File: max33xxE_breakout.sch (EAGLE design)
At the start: 4 parts

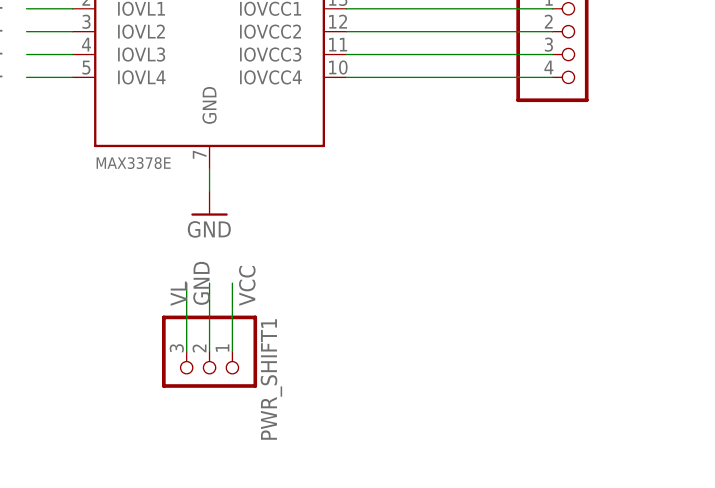
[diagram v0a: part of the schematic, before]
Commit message: rename the power segments too
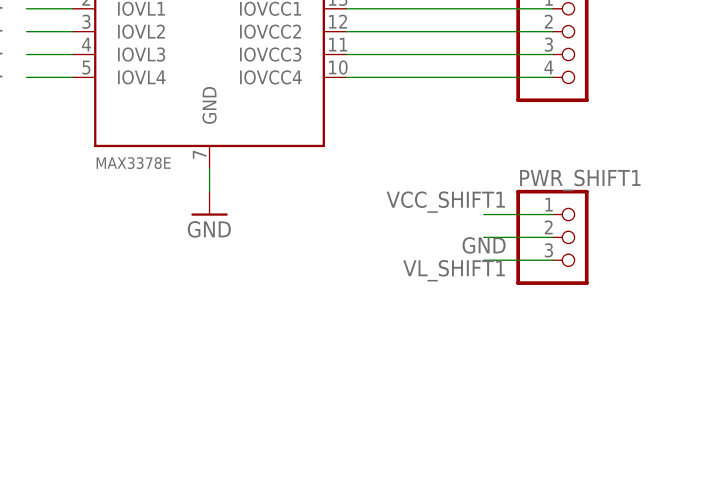
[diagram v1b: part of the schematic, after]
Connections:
- net VCC renamed VCC_SHIFT1
- net VL renamed VL_SHIFT1
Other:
- moved on the sheet: PWR_SHIFT1
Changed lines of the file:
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@@
 <instance part="P+1" gate="1" x="35.56" y="66.04"/>
 <instance part="+3V1" gate="G$1" x="30.48" y="66.04"/>
-<instance part="PWR_SHIFT1" gate="A" x="33.02" y="5.08" rot="R270"/>
+<instance part="PWR_SHIFT1" gate="A" x="73.66" y="20.32"/>
 <instance part="IOVCC_SHIFT1" gate="A" x="73.66" y="40.64"/>
 <instance part="IOVL_SHIFT1" gate="A" x="73.66" y="60.96"/>
@@
 <segment>
 <pinref part="PWR_SHIFT1" gate="A" pin="2"/>
-<wire x1="33.02" y1="7.62" x2="33.02" y2="15.24" width="0.1524" layer="91"/>
-<label x="33.02" y="12.7" size="1.778" layer="95" rot="R90"/>
+<wire x1="71.12" y1="20.32" x2="63.5" y2="20.32" width="0.1524" layer="91"/>
+<label x="66.04" y="20.32" size="1.778" layer="95" rot="R180"/>
 </segment>
 </net>
-<net name="VCC" class="0">
+<net name="VCC_SHIFT1" class="0">
 <segment>
 <pinref part="SHIFT1" gate="G$1" pin="VCC"/>
@@
 <segment>
 <pinref part="PWR_SHIFT1" gate="A" pin="1"/>
-<wire x1="35.56" y1="7.62" x2="35.56" y2="15.24" width="0.1524" layer="91"/>
-<label x="38.1" y="12.7" size="1.778" layer="95" rot="R90"/>
+<wire x1="71.12" y1="22.86" x2="63.5" y2="22.86" width="0.1524" layer="91"/>
+<label x="66.04" y="25.4" size="1.778" layer="95" rot="R180"/>
 </segment>
 </net>
-<net name="VL" class="0">
+<net name="VL_SHIFT1" class="0">
 <segment>
 <pinref part="SHIFT1" gate="G$1" pin="VL"/>
@@
 <segment>
 <pinref part="PWR_SHIFT1" gate="A" pin="3"/>
-<wire x1="30.48" y1="7.62" x2="30.48" y2="15.24" width="0.1524" layer="91"/>
-<label x="30.48" y="12.7" size="1.778" layer="95" rot="R90"/>
+<wire x1="71.12" y1="17.78" x2="63.5" y2="17.78" width="0.1524" layer="91"/>
+<label x="66.04" y="17.78" size="1.778" layer="95" rot="R180"/>
 </segment>
 </net>

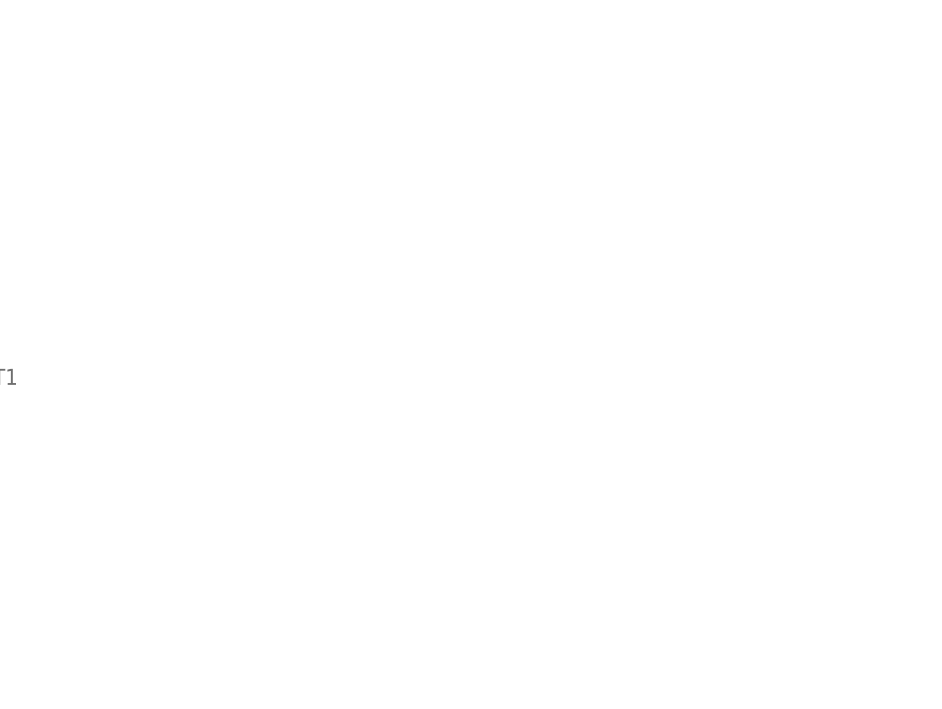
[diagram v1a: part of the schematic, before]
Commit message: apparently the automatic net rename when copying does not quite work if the nets are not actually drawn all the way through
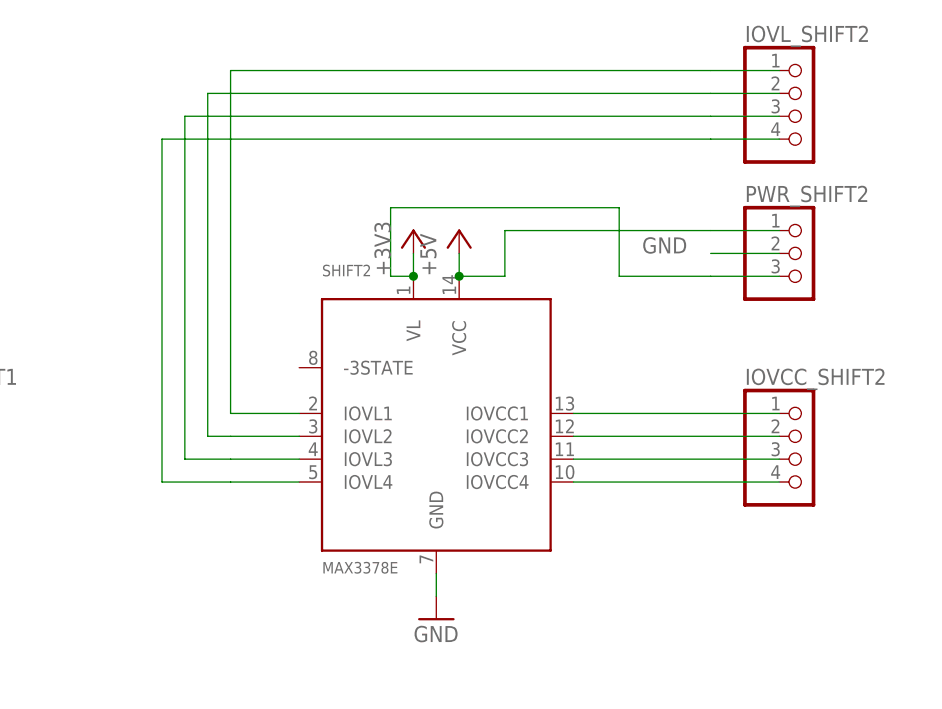
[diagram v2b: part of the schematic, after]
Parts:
- added IOVCC_SHIFT2, IOVL_SHIFT2: (no value), pinhead:PINHD-1X4
- added PWR_SHIFT2: (no value), pinhead:PINHD-1X3
- added SHIFT2: MAX3378E, max33xxE_lvl_shifters:MAX3378E
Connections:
- new net IOVCC1_SHIFT2: IOVCC_SHIFT2.1, SHIFT2.IOVCC1
- new net IOVCC2_SHIFT2: IOVCC_SHIFT2.2, SHIFT2.IOVCC2
- new net IOVCC3_SHIFT2: IOVCC_SHIFT2.3, SHIFT2.IOVCC3
- new net IOVCC4_SHIFT2: IOVCC_SHIFT2.4, SHIFT2.IOVCC4
- new net IOVL1_SHIFT2: IOVL_SHIFT2.1, SHIFT2.IOVL1
- new net IOVL2_SHIFT2: IOVL_SHIFT2.2, SHIFT2.IOVL2
- new net IOVL3_SHIFT2: IOVL_SHIFT2.3, SHIFT2.IOVL3
- new net IOVL4_SHIFT2: IOVL_SHIFT2.4, SHIFT2.IOVL4
- new net VCC_SHIFT2: PWR_SHIFT2.1, SHIFT2.VCC
- new net VL_SHIFT2: PWR_SHIFT2.3, SHIFT2.VL
- net GND: now also PWR_SHIFT2.2, SHIFT2.GND
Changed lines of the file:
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@@
 <part name="IOVCC_SHIFT1" library="pinhead" deviceset="PINHD-1X4" device=""/>
 <part name="IOVL_SHIFT1" library="pinhead" deviceset="PINHD-1X4" device=""/>
+<part name="SHIFT2" library="max33xxE_lvl_shifters" deviceset="MAX3378E" device=""/>
+<part name="GND2" library="supply1" deviceset="GND" device=""/>
+<part name="P+2" library="supply1" deviceset="+5V" device=""/>
+<part name="+3V2" library="supply1" deviceset="+3V3" device=""/>
+<part name="PWR_SHIFT2" library="pinhead" deviceset="PINHD-1X3" device=""/>
+<part name="IOVCC_SHIFT2" library="pinhead" deviceset="PINHD-1X4" device=""/>
+<part name="IOVL_SHIFT2" library="pinhead" deviceset="PINHD-1X4" device=""/>
 </parts>
 <sheets>
@@
 <instance part="IOVCC_SHIFT1" gate="A" x="73.66" y="40.64"/>
 <instance part="IOVL_SHIFT1" gate="A" x="73.66" y="60.96"/>
+<instance part="SHIFT2" gate="G$1" x="129.54" y="43.18"/>
+<instance part="GND2" gate="1" x="129.54" y="22.86"/>
+<instance part="P+2" gate="1" x="132.08" y="66.04"/>
+<instance part="+3V2" gate="G$1" x="127" y="66.04"/>
+<instance part="PWR_SHIFT2" gate="A" x="170.18" y="63.5"/>
+<instance part="IOVCC_SHIFT2" gate="A" x="170.18" y="40.64"/>
+<instance part="IOVL_SHIFT2" gate="A" x="170.18" y="78.74"/>
 </instances>
 <busses>
@@
 <label x="66.04" y="20.32" size="1.778" layer="95" rot="R180"/>
 </segment>
+<segment>
+<pinref part="SHIFT2" gate="G$1" pin="GND"/>
+<pinref part="GND2" gate="1" pin="GND"/>
+<wire x1="129.54" y1="25.4" x2="129.54" y2="27.94" width="0.1524" layer="91"/>
+</segment>
+<segment>
+<pinref part="PWR_SHIFT2" gate="A" pin="2"/>
+<wire x1="167.64" y1="63.5" x2="160.02" y2="63.5" width="0.1524" layer="91"/>
+<label x="152.4" y="63.5" size="1.778" layer="95"/>
+</segment>
 </net>
 <net name="VCC_SHIFT1" class="0">
@@
 </segment>
 </net>
+<net name="IOVCC4_SHIFT2" class="0">
+<segment>
+<pinref part="SHIFT2" gate="G$1" pin="IOVCC4"/>
+<pinref part="IOVCC_SHIFT2" gate="A" pin="4"/>
+<wire x1="144.78" y1="38.1" x2="167.64" y2="38.1" width="0.1524" layer="91"/>
+</segment>
+</net>
+<net name="IOVCC3_SHIFT2" class="0">
+<segment>
+<pinref part="SHIFT2" gate="G$1" pin="IOVCC3"/>
+<pinref part="IOVCC_SHIFT2" gate="A" pin="3"/>
+<wire x1="144.78" y1="40.64" x2="167.64" y2="40.64" width="0.1524" layer="91"/>
+</segment>
+</net>
+<net name="IOVCC2_SHIFT2" class="0">
+<segment>
+<pinref part="SHIFT2" gate="G$1" pin="IOVCC2"/>
+<pinref part="IOVCC_SHIFT2" gate="A" pin="2"/>
+<wire x1="144.78" y1="43.18" x2="167.64" y2="43.18" width="0.1524" layer="91"/>
+</segment>
+</net>
+<net name="IOVCC1_SHIFT2" class="0">
+<segment>
+<pinref part="SHIFT2" gate="G$1" pin="IOVCC1"/>
+<pinref part="IOVCC_SHIFT2" gate="A" pin="1"/>
+<wire x1="144.78" y1="45.72" x2="167.64" y2="45.72" width="0.1524" layer="91"/>
+</segment>
+</net>
+<net name="IOVL2_SHIFT2" class="0">
+<segment>
+<pinref part="IOVL_SHIFT2" gate="A" pin="2"/>
+<wire x1="167.64" y1="81.28" x2="160.02" y2="81.28" width="0.1524" layer="91"/>
+<wire x1="160.02" y1="81.28" x2="104.14" y2="81.28" width="0.1524" layer="91"/>
+<wire x1="104.14" y1="81.28" x2="104.14" y2="43.18" width="0.1524" layer="91"/>
+<pinref part="SHIFT2" gate="G$1" pin="IOVL2"/>
+<wire x1="114.3" y1="43.18" x2="106.68" y2="43.18" width="0.1524" layer="91"/>
+<wire x1="104.14" y1="43.18" x2="106.68" y2="43.18" width="0.1524" layer="91"/>
+</segment>
+</net>
+<net name="IOVL1_SHIFT2" class="0">
+<segment>
+<pinref part="IOVL_SHIFT2" gate="A" pin="1"/>
+<wire x1="167.64" y1="83.82" x2="160.02" y2="83.82" width="0.1524" layer="91"/>
+<pinref part="SHIFT2" gate="G$1" pin="IOVL1"/>
+<wire x1="114.3" y1="45.72" x2="106.68" y2="45.72" width="0.1524" layer="91"/>
+<wire x1="160.02" y1="83.82" x2="106.68" y2="83.82" width="0.1524" layer="91"/>
+<wire x1="106.68" y1="83.82" x2="106.68" y2="45.72" width="0.1524" layer="91"/>
+</segment>
+</net>
+<net name="IOVL3_SHIFT2" class="0">
+<segment>
+<pinref part="IOVL_SHIFT2" gate="A" pin="3"/>
+<wire x1="167.64" y1="78.74" x2="160.02" y2="78.74" width="0.1524" layer="91"/>
+<wire x1="160.02" y1="78.74" x2="101.6" y2="78.74" width="0.1524" layer="91"/>
+<wire x1="101.6" y1="78.74" x2="101.6" y2="40.64" width="0.1524" layer="91"/>
+<pinref part="SHIFT2" gate="G$1" pin="IOVL3"/>
+<wire x1="114.3" y1="40.64" x2="106.68" y2="40.64" width="0.1524" layer="91"/>
+<wire x1="101.6" y1="40.64" x2="106.68" y2="40.64" width="0.1524" layer="91"/>
+</segment>
+</net>
+<net name="IOVL4_SHIFT2" class="0">
+<segment>
+<pinref part="IOVL_SHIFT2" gate="A" pin="4"/>
+<wire x1="167.64" y1="76.2" x2="160.02" y2="76.2" width="0.1524" layer="91"/>
+<wire x1="160.02" y1="76.2" x2="99.06" y2="76.2" width="0.1524" layer="91"/>
+<wire x1="99.06" y1="76.2" x2="99.06" y2="38.1" width="0.1524" layer="91"/>
+<pinref part="SHIFT2" gate="G$1" pin="IOVL4"/>
+<wire x1="114.3" y1="38.1" x2="106.68" y2="38.1" width="0.1524" layer="91"/>
+<wire x1="99.06" y1="38.1" x2="106.68" y2="38.1" width="0.1524" layer="91"/>
+</segment>
+</net>
+<net name="VL_SHIFT2" class="0">
+<segment>
+<pinref part="SHIFT2" gate="G$1" pin="VL"/>
+<pinref part="+3V2" gate="G$1" pin="+3V3"/>
+<wire x1="127" y1="63.5" x2="127" y2="60.96" width="0.1524" layer="91"/>
+<pinref part="PWR_SHIFT2" gate="A" pin="3"/>
+<wire x1="167.64" y1="60.96" x2="160.02" y2="60.96" width="0.1524" layer="91"/>
+<wire x1="160.02" y1="60.96" x2="149.86" y2="60.96" width="0.1524" layer="91"/>
+<wire x1="149.86" y1="60.96" x2="149.86" y2="68.58" width="0.1524" layer="91"/>
+<wire x1="149.86" y1="68.58" x2="124.46" y2="68.58" width="0.1524" layer="91"/>
+<wire x1="124.46" y1="68.58" x2="124.46" y2="60.96" width="0.1524" layer="91"/>
+<wire x1="124.46" y1="60.96" x2="127" y2="60.96" width="0.1524" layer="91"/>
+<junction x="127" y="60.96"/>
+</segment>
+</net>
+<net name="VCC_SHIFT2" class="0">
+<segment>
+<pinref part="SHIFT2" gate="G$1" pin="VCC"/>
+<pinref part="P+2" gate="1" pin="+5V"/>
+<wire x1="132.08" y1="63.5" x2="132.08" y2="60.96" width="0.1524" layer="91"/>
+<pinref part="PWR_SHIFT2" gate="A" pin="1"/>
+<wire x1="167.64" y1="66.04" x2="160.02" y2="66.04" width="0.1524" layer="91"/>
+<wire x1="160.02" y1="66.04" x2="137.16" y2="66.04" width="0.1524" layer="91"/>
+<wire x1="137.16" y1="66.04" x2="137.16" y2="60.96" width="0.1524" layer="91"/>
+<wire x1="137.16" y1="60.96" x2="132.08" y2="60.96" width="0.1524" layer="91"/>
+<junction x="132.08" y="60.96"/>
+</segment>
+</net>

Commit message: quick first placement
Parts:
- added IOVCC_SHIFT3, IOVL_SHIFT3: (no value), pinhead:PINHD-1X4
- added PWR_SHIFT3: (no value), pinhead:PINHD-1X3
- added SHIFT3: MAX3378E, max33xxE_lvl_shifters:MAX3378E
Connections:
- new net IOVCC1_SHIFT3: IOVCC_SHIFT3.1, SHIFT3.IOVCC1
- new net IOVCC2_SHIFT3: IOVCC_SHIFT3.2, SHIFT3.IOVCC2
- new net IOVCC3_SHIFT3: IOVCC_SHIFT3.3, SHIFT3.IOVCC3
- new net IOVCC4_SHIFT3: IOVCC_SHIFT3.4, SHIFT3.IOVCC4
- new net IOVL1_SHIFT3: IOVL_SHIFT3.1, SHIFT3.IOVL1
- new net IOVL2_SHIFT3: IOVL_SHIFT3.2, SHIFT3.IOVL2
- new net IOVL3_SHIFT3: IOVL_SHIFT3.3, SHIFT3.IOVL3
- new net IOVL4_SHIFT3: IOVL_SHIFT3.4, SHIFT3.IOVL4
- new net VCC_SHIFT3: PWR_SHIFT3.1, SHIFT3.VCC
- new net VL_SHIFT3: PWR_SHIFT3.3, SHIFT3.VL
- net GND: now also PWR_SHIFT3.2, SHIFT3.GND
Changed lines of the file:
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@@
 <part name="IOVCC_SHIFT2" library="pinhead" deviceset="PINHD-1X4" device=""/>
 <part name="IOVL_SHIFT2" library="pinhead" deviceset="PINHD-1X4" device=""/>
+<part name="SHIFT3" library="max33xxE_lvl_shifters" deviceset="MAX3378E" device=""/>
+<part name="GND3" library="supply1" deviceset="GND" device=""/>
+<part name="P+3" library="supply1" deviceset="+5V" device=""/>
+<part name="+3V3" library="supply1" deviceset="+3V3" device=""/>
+<part name="PWR_SHIFT3" library="pinhead" deviceset="PINHD-1X3" device=""/>
+<part name="IOVCC_SHIFT3" library="pinhead" deviceset="PINHD-1X4" device=""/>
+<part name="IOVL_SHIFT3" library="pinhead" deviceset="PINHD-1X4" device=""/>
 </parts>
 <sheets>
@@
 <instance part="IOVCC_SHIFT2" gate="A" x="170.18" y="40.64"/>
 <instance part="IOVL_SHIFT2" gate="A" x="170.18" y="78.74"/>
+<instance part="SHIFT3" gate="G$1" x="226.06" y="38.1"/>
+<instance part="GND3" gate="1" x="226.06" y="17.78"/>
+<instance part="P+3" gate="1" x="228.6" y="60.96"/>
+<instance part="+3V3" gate="G$1" x="223.52" y="60.96"/>
+<instance part="PWR_SHIFT3" gate="A" x="266.7" y="58.42"/>
+<instance part="IOVCC_SHIFT3" gate="A" x="266.7" y="35.56"/>
+<instance part="IOVL_SHIFT3" gate="A" x="266.7" y="73.66"/>
 </instances>
 <busses>
@@
 <wire x1="167.64" y1="63.5" x2="160.02" y2="63.5" width="0.1524" layer="91"/>
 <label x="152.4" y="63.5" size="1.778" layer="95"/>
+</segment>
+<segment>
+<pinref part="SHIFT3" gate="G$1" pin="GND"/>
+<pinref part="GND3" gate="1" pin="GND"/>
+<wire x1="226.06" y1="20.32" x2="226.06" y2="22.86" width="0.1524" layer="91"/>
+</segment>
+<segment>
+<pinref part="PWR_SHIFT3" gate="A" pin="2"/>
+<wire x1="264.16" y1="58.42" x2="256.54" y2="58.42" width="0.1524" layer="91"/>
+<label x="248.92" y="58.42" size="1.778" layer="95"/>
 </segment>
 </net>
@@
 </segment>
 </net>
+<net name="IOVCC4_SHIFT3" class="0">
+<segment>
+<pinref part="SHIFT3" gate="G$1" pin="IOVCC4"/>
+<pinref part="IOVCC_SHIFT3" gate="A" pin="4"/>
+<wire x1="241.3" y1="33.02" x2="264.16" y2="33.02" width="0.1524" layer="91"/>
+</segment>
+</net>
+<net name="IOVCC3_SHIFT3" class="0">
+<segment>
+<pinref part="SHIFT3" gate="G$1" pin="IOVCC3"/>
+<pinref part="IOVCC_SHIFT3" gate="A" pin="3"/>
+<wire x1="241.3" y1="35.56" x2="264.16" y2="35.56" width="0.1524" layer="91"/>
+</segment>
+</net>
+<net name="IOVCC2_SHIFT3" class="0">
+<segment>
+<pinref part="SHIFT3" gate="G$1" pin="IOVCC2"/>
+<pinref part="IOVCC_SHIFT3" gate="A" pin="2"/>
+<wire x1="241.3" y1="38.1" x2="264.16" y2="38.1" width="0.1524" layer="91"/>
+</segment>
+</net>
+<net name="IOVCC1_SHIFT3" class="0">
+<segment>
+<pinref part="SHIFT3" gate="G$1" pin="IOVCC1"/>
+<pinref part="IOVCC_SHIFT3" gate="A" pin="1"/>
+<wire x1="241.3" y1="40.64" x2="264.16" y2="40.64" width="0.1524" layer="91"/>
+</segment>
+</net>
+<net name="IOVL2_SHIFT3" class="0">
+<segment>
+<pinref part="IOVL_SHIFT3" gate="A" pin="2"/>
+<wire x1="264.16" y1="76.2" x2="256.54" y2="76.2" width="0.1524" layer="91"/>
+<wire x1="256.54" y1="76.2" x2="200.66" y2="76.2" width="0.1524" layer="91"/>
+<wire x1="200.66" y1="76.2" x2="200.66" y2="38.1" width="0.1524" layer="91"/>
+<pinref part="SHIFT3" gate="G$1" pin="IOVL2"/>
+<wire x1="210.82" y1="38.1" x2="203.2" y2="38.1" width="0.1524" layer="91"/>
+<wire x1="200.66" y1="38.1" x2="203.2" y2="38.1" width="0.1524" layer="91"/>
+</segment>
+</net>
+<net name="IOVL1_SHIFT3" class="0">
+<segment>
+<pinref part="IOVL_SHIFT3" gate="A" pin="1"/>
+<wire x1="264.16" y1="78.74" x2="256.54" y2="78.74" width="0.1524" layer="91"/>
+<pinref part="SHIFT3" gate="G$1" pin="IOVL1"/>
+<wire x1="210.82" y1="40.64" x2="203.2" y2="40.64" width="0.1524" layer="91"/>
+<wire x1="256.54" y1="78.74" x2="203.2" y2="78.74" width="0.1524" layer="91"/>
+<wire x1="203.2" y1="78.74" x2="203.2" y2="40.64" width="0.1524" layer="91"/>
+</segment>
+</net>
+<net name="IOVL3_SHIFT3" class="0">
+<segment>
+<pinref part="IOVL_SHIFT3" gate="A" pin="3"/>
+<wire x1="264.16" y1="73.66" x2="256.54" y2="73.66" width="0.1524" layer="91"/>
+<wire x1="256.54" y1="73.66" x2="198.12" y2="73.66" width="0.1524" layer="91"/>
+<wire x1="198.12" y1="73.66" x2="198.12" y2="35.56" width="0.1524" layer="91"/>
+<pinref part="SHIFT3" gate="G$1" pin="IOVL3"/>
+<wire x1="210.82" y1="35.56" x2="203.2" y2="35.56" width="0.1524" layer="91"/>
+<wire x1="198.12" y1="35.56" x2="203.2" y2="35.56" width="0.1524" layer="91"/>
+</segment>
+</net>
+<net name="IOVL4_SHIFT3" class="0">
+<segment>
+<pinref part="IOVL_SHIFT3" gate="A" pin="4"/>
+<wire x1="264.16" y1="71.12" x2="256.54" y2="71.12" width="0.1524" layer="91"/>
+<wire x1="256.54" y1="71.12" x2="195.58" y2="71.12" width="0.1524" layer="91"/>
+<wire x1="195.58" y1="71.12" x2="195.58" y2="33.02" width="0.1524" layer="91"/>
+<pinref part="SHIFT3" gate="G$1" pin="IOVL4"/>
+<wire x1="210.82" y1="33.02" x2="203.2" y2="33.02" width="0.1524" layer="91"/>
+<wire x1="195.58" y1="33.02" x2="203.2" y2="33.02" width="0.1524" layer="91"/>
+</segment>
+</net>
+<net name="VL_SHIFT3" class="0">
+<segment>
+<pinref part="SHIFT3" gate="G$1" pin="VL"/>
+<pinref part="+3V3" gate="G$1" pin="+3V3"/>
+<wire x1="223.52" y1="58.42" x2="223.52" y2="55.88" width="0.1524" layer="91"/>
+<pinref part="PWR_SHIFT3" gate="A" pin="3"/>
+<wire x1="264.16" y1="55.88" x2="256.54" y2="55.88" width="0.1524" layer="91"/>
+<wire x1="256.54" y1="55.88" x2="246.38" y2="55.88" width="0.1524" layer="91"/>
+<wire x1="246.38" y1="55.88" x2="246.38" y2="63.5" width="0.1524" layer="91"/>
+<wire x1="246.38" y1="63.5" x2="220.98" y2="63.5" width="0.1524" layer="91"/>
+<wire x1="220.98" y1="63.5" x2="220.98" y2="55.88" width="0.1524" layer="91"/>
+<wire x1="220.98" y1="55.88" x2="223.52" y2="55.88" width="0.1524" layer="91"/>
+<junction x="223.52" y="55.88"/>
+</segment>
+</net>
+<net name="VCC_SHIFT3" class="0">
+<segment>
+<pinref part="SHIFT3" gate="G$1" pin="VCC"/>
+<pinref part="P+3" gate="1" pin="+5V"/>
+<wire x1="228.6" y1="58.42" x2="228.6" y2="55.88" width="0.1524" layer="91"/>
+<pinref part="PWR_SHIFT3" gate="A" pin="1"/>
+<wire x1="264.16" y1="60.96" x2="256.54" y2="60.96" width="0.1524" layer="91"/>
+<wire x1="256.54" y1="60.96" x2="233.68" y2="60.96" width="0.1524" layer="91"/>
+<wire x1="233.68" y1="60.96" x2="233.68" y2="55.88" width="0.1524" layer="91"/>
+<wire x1="233.68" y1="55.88" x2="228.6" y2="55.88" width="0.1524" layer="91"/>
+<junction x="228.6" y="55.88"/>
+</segment>
+</net>
